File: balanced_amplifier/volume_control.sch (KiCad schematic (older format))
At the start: 49 parts, among them U5 LM4562, U6 LM4562, U7 LM4562, U8 LM4562

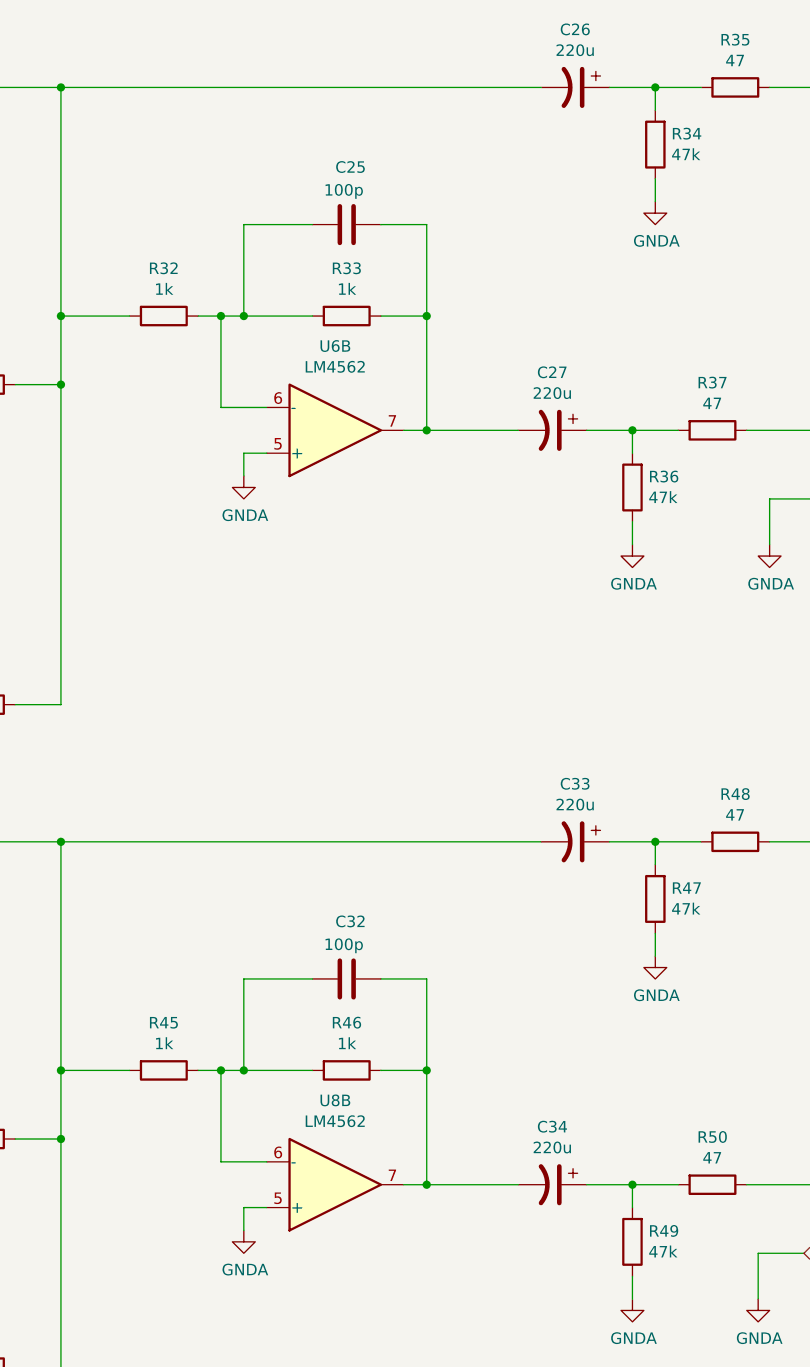
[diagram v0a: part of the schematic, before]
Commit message: Update output coupling cap to be nonpolarized and add specific part details
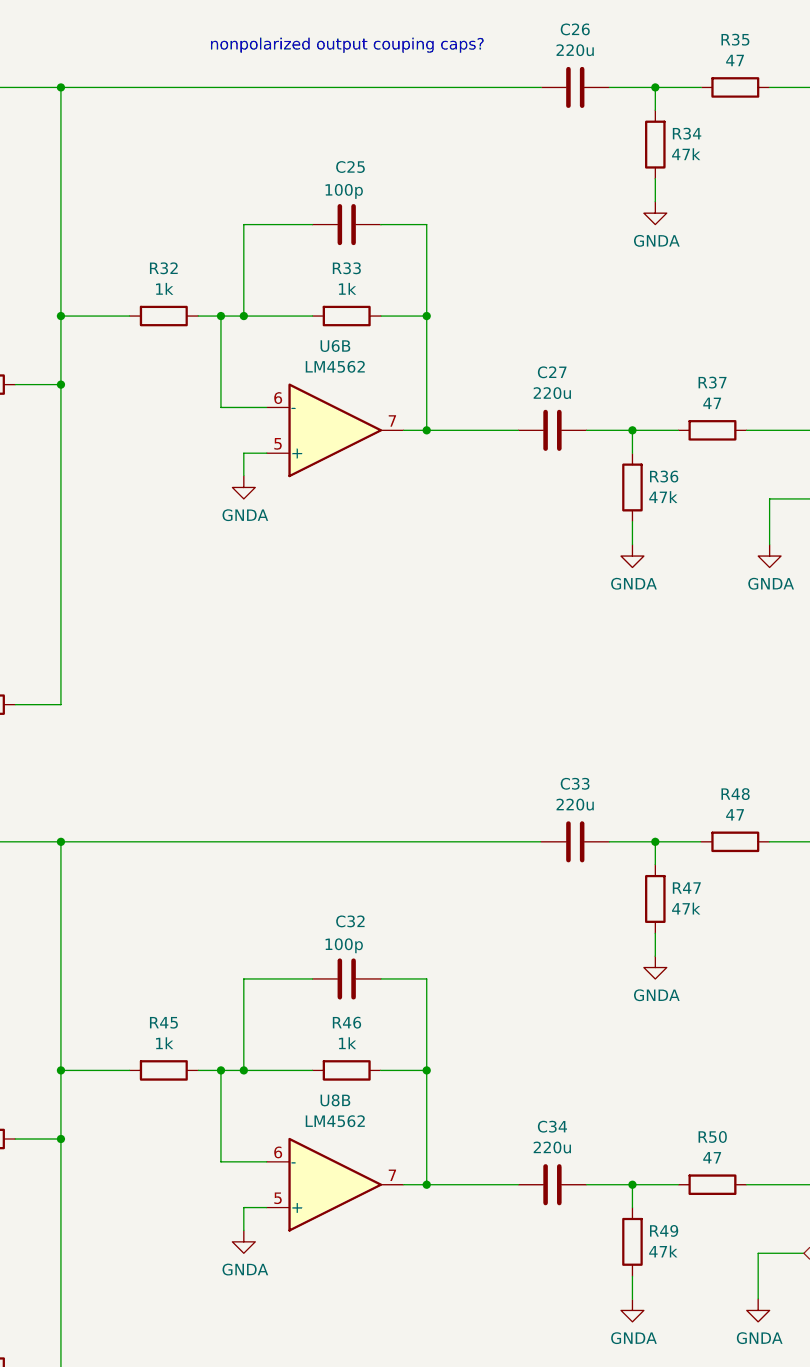
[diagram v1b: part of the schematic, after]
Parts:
- removed C26, C27, C33, C34: 220u, symbol Device:CP1
- added C26, C27, C33, C34: 220u, Capacitor_THT:C_Radial_D12.5mm_H25.0mm_P5.00mm, symbol Device:C
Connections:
- net at C25.1, R33.1, U6.7: now also C27.2
- net at R28.1, R31.1, R32.2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: now also C26.2
- net at C32.1, R46.1, U8.7: now also C34.2
- net at R41.1, R44.1, R45.2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: now also C33.2
- net at R34.2, R35.2: now also C26.1
- net at R36.2, R37.2: now also C27.1
- net at R49.2, R50.2: now also C34.1
- net at R47.2, R48.2: now also C33.1
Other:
- note added: "nonpolarized output couping caps?"
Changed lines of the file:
@@
 	8050 5200 8050 4800
-$Comp
-L Device:CP1 C34
-U 1 1 5C15C581
-P 8600 5700
-F 0 "C34" V 8348 5700 50  0000 C CNN
-F 1 "220u" V 8439 5700 50  0000 C CNN
-F 2 "" H 8600 5700 50  0001 C CNN
-F 3 "~" H 8600 5700 50  0001 C CNN
-F 4 "Electrolytic" V 8600 5700 50  0001 C CNN "Dielectric"
-F 5 "35V" V 8600 5700 50  0001 C CNN "Voltage Rating"
-	1    8600 5700
-	0    1    1    0
-$EndComp
 $Comp
 L Device:R R49
@@
 	0    -1   -1   0
 $EndComp
-$Comp
-L Device:CP1 C33
-U 1 1 5C4F3941
+Text Notes 7100 750  0    50   ~ 0
+nonpolarized output couping caps?
+$Comp
+L Device:C C?
+U 1 1 5C4F8306
+P 8700 900
+AR Path="/5C4F8306" Ref="C?"  Part="1"
+AR Path="/5BE4EEC1/5C4F8306" Ref="C?"  Part="1"
+AR Path="/5BF8808C/5C4F8306" Ref="C26"  Part="1"
+F 0 "C26" V 8448 900 50  0000 C CNN
+F 1 "220u" V 8539 900 50  0000 C CNN
+F 2 "Capacitor_THT:C_Radial_D12.5mm_H25.0mm_P5.00mm" H 8738 750 50  0001 C CNN
+F 3 "http://nichicon-us.com/english/products/pdfs/e-uvp.pdf" H 8700 900 50  0001 C CNN
+F 4 "Nichicon" H 8700 900 50  0001 C CNN "Manufacturer"
+F 5 "UVP1V221MHD" H 8700 900 50  0001 C CNN "Manufacturer PN"
+F 6 "Digikey" H 8700 900 50  0001 C CNN "Distributor"
+F 7 "493-16138-ND" H 8700 900 50  0001 C CNN "Distributor PN"
+F 8 "https://www.digikey.com/product-detail/en/nichicon/UVP1V221MHD/493-16138-ND/2539596" H 8700 900 50  0001 C CNN "URL"
+F 9 "0.87" H 8700 900 50  0001 C CNN "Unit Price"
+F 10 "Nonpolarized Electrolytic" V 8700 900 50  0001 C CNN "Dielectric"
+F 11 "35V" V 8700 900 50  0001 C CNN "Voltage Rating"
+	1    8700 900
+	0    1    1    0
+$EndComp
+$Comp
+L Device:C C?
+U 1 1 5C503D82
+P 8600 2400
+AR Path="/5C503D82" Ref="C?"  Part="1"
+AR Path="/5BE4EEC1/5C503D82" Ref="C?"  Part="1"
+AR Path="/5BF8808C/5C503D82" Ref="C27"  Part="1"
+F 0 "C27" V 8348 2400 50  0000 C CNN
+F 1 "220u" V 8439 2400 50  0000 C CNN
+F 2 "Capacitor_THT:C_Radial_D12.5mm_H25.0mm_P5.00mm" H 8638 2250 50  0001 C CNN
+F 3 "http://nichicon-us.com/english/products/pdfs/e-uvp.pdf" H 8600 2400 50  0001 C CNN
+F 4 "Nichicon" H 8600 2400 50  0001 C CNN "Manufacturer"
+F 5 "UVP1V221MHD" H 8600 2400 50  0001 C CNN "Manufacturer PN"
+F 6 "Digikey" H 8600 2400 50  0001 C CNN "Distributor"
+F 7 "493-16138-ND" H 8600 2400 50  0001 C CNN "Distributor PN"
+F 8 "https://www.digikey.com/product-detail/en/nichicon/UVP1V221MHD/493-16138-ND/2539596" H 8600 2400 50  0001 C CNN "URL"
+F 9 "0.87" H 8600 2400 50  0001 C CNN "Unit Price"
+F 10 "Nonpolarized Electrolytic" V 8600 2400 50  0001 C CNN "Dielectric"
+F 11 "35V" V 8600 2400 50  0001 C CNN "Voltage Rating"
+	1    8600 2400
+	0    1    1    0
+$EndComp
+$Comp
+L Device:C C?
+U 1 1 5C503F94
 P 8700 4200
+AR Path="/5C503F94" Ref="C?"  Part="1"
+AR Path="/5BE4EEC1/5C503F94" Ref="C?"  Part="1"
+AR Path="/5BF8808C/5C503F94" Ref="C33"  Part="1"
 F 0 "C33" V 8448 4200 50  0000 C CNN
 F 1 "220u" V 8539 4200 50  0000 C CNN
-F 2 "" H 8700 4200 50  0001 C CNN
-F 3 "~" H 8700 4200 50  0001 C CNN
-F 4 "Electrolytic" V 8700 4200 50  0001 C CNN "Dielectric"
-F 5 "35V" V 8700 4200 50  0001 C CNN "Voltage Rating"
+F 2 "Capacitor_THT:C_Radial_D12.5mm_H25.0mm_P5.00mm" H 8738 4050 50  0001 C CNN
+F 3 "http://nichicon-us.com/english/products/pdfs/e-uvp.pdf" H 8700 4200 50  0001 C CNN
+F 4 "Nichicon" H 8700 4200 50  0001 C CNN "Manufacturer"
+F 5 "UVP1V221MHD" H 8700 4200 50  0001 C CNN "Manufacturer PN"
+F 6 "Digikey" H 8700 4200 50  0001 C CNN "Distributor"
+F 7 "493-16138-ND" H 8700 4200 50  0001 C CNN "Distributor PN"
+F 8 "https://www.digikey.com/product-detail/en/nichicon/UVP1V221MHD/493-16138-ND/2539596" H 8700 4200 50  0001 C CNN "URL"
+F 9 "0.87" H 8700 4200 50  0001 C CNN "Unit Price"
+F 10 "Nonpolarized Electrolytic" V 8700 4200 50  0001 C CNN "Dielectric"
+F 11 "35V" V 8700 4200 50  0001 C CNN "Voltage Rating"
 	1    8700 4200
 	0    1    1    0
 $EndComp
 $Comp
-L Device:CP1 C27
-U 1 1 5C4F39DA
-P 8600 2400
-F 0 "C27" V 8348 2400 50  0000 C CNN
-F 1 "220u" V 8439 2400 50  0000 C CNN
-F 2 "" H 8600 2400 50  0001 C CNN
-F 3 "~" H 8600 2400 50  0001 C CNN
-F 4 "Electrolytic" V 8600 2400 50  0001 C CNN "Dielectric"
-F 5 "35V" V 8600 2400 50  0001 C CNN "Voltage Rating"
-	1    8600 2400
-	0    1    1    0
-$EndComp
-$Comp
-L Device:CP1 C26
-U 1 1 5C4F3A7A
-P 8700 900
-F 0 "C26" V 8448 900 50  0000 C CNN
-F 1 "220u" V 8539 900 50  0000 C CNN
-F 2 "" H 8700 900 50  0001 C CNN
-F 3 "~" H 8700 900 50  0001 C CNN
-F 4 "Electrolytic" V 8700 900 50  0001 C CNN "Dielectric"
-F 5 "35V" V 8700 900 50  0001 C CNN "Voltage Rating"
-	1    8700 900
-	0    1    1    0
-$EndComp
+L Device:C C?
+U 1 1 5C50403E
+P 8600 5700
+AR Path="/5C50403E" Ref="C?"  Part="1"
+AR Path="/5BE4EEC1/5C50403E" Ref="C?"  Part="1"
+AR Path="/5BF8808C/5C50403E" Ref="C34"  Part="1"
+F 0 "C34" V 8348 5700 50  0000 C CNN
+F 1 "220u" V 8439 5700 50  0000 C CNN
+F 2 "Capacitor_THT:C_Radial_D12.5mm_H25.0mm_P5.00mm" H 8638 5550 50  0001 C CNN
+F 3 "http://nichicon-us.com/english/products/pdfs/e-uvp.pdf" H 8600 5700 50  0001 C CNN
+F 4 "Nichicon" H 8600 5700 50  0001 C CNN "Manufacturer"
+F 5 "UVP1V221MHD" H 8600 5700 50  0001 C CNN "Manufacturer PN"
+F 6 "Digikey" H 8600 5700 50  0001 C CNN "Distributor"
+F 7 "493-16138-ND" H 8600 5700 50  0001 C CNN "Distributor PN"
+F 8 "https://www.digikey.com/product-detail/en/nichicon/UVP1V221MHD/493-16138-ND/2539596" H 8600 5700 50  0001 C CNN "URL"
+F 9 "0.87" H 8600 5700 50  0001 C CNN "Unit Price"
+F 10 "Nonpolarized Electrolytic" V 8600 5700 50  0001 C CNN "Dielectric"
+F 11 "35V" V 8600 5700 50  0001 C CNN "Voltage Rating"
+	1    8600 5700
+	0    1    1    0
+$EndComp

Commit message: add specific part details to capacitors
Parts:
- C22, C29: footprint (none) -> Capacitor_THT:CP_Radial_D5.0mm_P2.00mm; Distributor (none) -> Digikey; Distributor PN (none) -> 493-1077-ND; Manufacturer (none) -> Nichicon; Manufacturer PN (none) -> UVR1V100MDD; URL (none) -> https://www.digikey.com/product-detail/en/nichicon/UVR1V100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; Unit Price (none) -> 0.27
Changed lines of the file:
@@
 F 0 "C22" V 3252 1800 50  0000 C CNN
 F 1 "10u" V 3161 1800 50  0000 C CNN
-F 2 "" H 3000 1800 50  0001 C CNN
-F 3 "~" H 3000 1800 50  0001 C CNN
-F 4 "Electrolytic" V 3000 1800 50  0001 C CNN "Dielectric"
-F 5 "35V" V 3000 1800 50  0001 C CNN "Voltage Rating"
+F 2 "Capacitor_THT:CP_Radial_D5.0mm_P2.00mm" H 3000 1800 50  0001 C CNN
+F 3 "http://nichicon-us.com/english/products/pdfs/e-uvr.pdf" H 3000 1800 50  0001 C CNN
+F 4 "Nichicon" H 3000 1800 50  0001 C CNN "Manufacturer"
+F 5 "UVR1V100MDD" H 3000 1800 50  0001 C CNN "Manufacturer PN"
+F 6 "Digikey" H 3000 1800 50  0001 C CNN "Distributor"
+F 7 "493-1077-ND" H 3000 1800 50  0001 C CNN "Distributor PN"
+F 8 "https://www.digikey.com/product-detail/en/nichicon/UVR1V100MDD/493-1077-ND/588818" H 3000 1800 50  0001 C CNN "URL"
+F 9 "0.27" H 3000 1800 50  0001 C CNN "Unit Price"
+F 10 "Electrolytic" V 3000 1800 50  0001 C CNN "Dielectric"
+F 11 "35V" V 3000 1800 50  0001 C CNN "Voltage Rating"
 	1    3000 1800
 	0    -1   -1   0
@@
 F 1 "100p" V 5150 1200 50  0000 L CNN
 F 2 "Capacitor_SMD:C_0603_1608Metric_Pad1.05x0.95mm_HandSolder" H 5338 1150 50  0001 C CNN
-F 3 "~" H 5300 1300 50  0001 C CNN
+F 3 "http://www.yageo.com/documents/recent/UPY-GP_NP0_16V-to-50V_16.pdf" H 5300 1300 50  0001 C CNN
 F 4 "Yageo" H 5300 1300 50  0001 C CNN "Manufacturer"
 F 5 "CC0603JRNPO9BN101" H 5300 1300 50  0001 C CNN "Manufacturer PN"
@@
 F 1 "100p" V 5150 2600 50  0000 L CNN
 F 2 "Capacitor_SMD:C_0603_1608Metric_Pad1.05x0.95mm_HandSolder" H 5338 2550 50  0001 C CNN
-F 3 "~" H 5300 2700 50  0001 C CNN
+F 3 "http://www.yageo.com/documents/recent/UPY-GP_NP0_16V-to-50V_16.pdf" H 5300 2700 50  0001 C CNN
 F 4 "Yageo" H 5300 2700 50  0001 C CNN "Manufacturer"
 F 5 "CC0603JRNPO9BN101" H 5300 2700 50  0001 C CNN "Manufacturer PN"
@@
 F 1 "100p" V 7550 1400 50  0000 L CNN
 F 2 "Capacitor_SMD:C_0603_1608Metric_Pad1.05x0.95mm_HandSolder" H 7738 1350 50  0001 C CNN
-F 3 "~" H 7700 1500 50  0001 C CNN
+F 3 "http://www.yageo.com/documents/recent/UPY-GP_NP0_16V-to-50V_16.pdf" H 7700 1500 50  0001 C CNN
 F 4 "Yageo" H 7700 1500 50  0001 C CNN "Manufacturer"
 F 5 "CC0603JRNPO9BN101" H 7700 1500 50  0001 C CNN "Manufacturer PN"
@@
 F 1 "100p" V 5150 4500 50  0000 L CNN
 F 2 "Capacitor_SMD:C_0603_1608Metric_Pad1.05x0.95mm_HandSolder" H 5338 4450 50  0001 C CNN
-F 3 "~" H 5300 4600 50  0001 C CNN
+F 3 "http://www.yageo.com/documents/recent/UPY-GP_NP0_16V-to-50V_16.pdf" H 5300 4600 50  0001 C CNN
 F 4 "Yageo" H 5300 4600 50  0001 C CNN "Manufacturer"
 F 5 "CC0603JRNPO9BN101" H 5300 4600 50  0001 C CNN "Manufacturer PN"
@@
 F 1 "100p" V 5150 5900 50  0000 L CNN
 F 2 "Capacitor_SMD:C_0603_1608Metric_Pad1.05x0.95mm_HandSolder" H 5338 5850 50  0001 C CNN
-F 3 "~" H 5300 6000 50  0001 C CNN
+F 3 "http://www.yageo.com/documents/recent/UPY-GP_NP0_16V-to-50V_16.pdf" H 5300 6000 50  0001 C CNN
 F 4 "Yageo" H 5300 6000 50  0001 C CNN "Manufacturer"
 F 5 "CC0603JRNPO9BN101" H 5300 6000 50  0001 C CNN "Manufacturer PN"
@@
 F 1 "100p" V 7550 4700 50  0000 L CNN
 F 2 "Capacitor_SMD:C_0603_1608Metric_Pad1.05x0.95mm_HandSolder" H 7738 4650 50  0001 C CNN
-F 3 "~" H 7700 4800 50  0001 C CNN
+F 3 "http://www.yageo.com/documents/recent/UPY-GP_NP0_16V-to-50V_16.pdf" H 7700 4800 50  0001 C CNN
 F 4 "Yageo" H 7700 4800 50  0001 C CNN "Manufacturer"
 F 5 "CC0603JRNPO9BN101" H 7700 4800 50  0001 C CNN "Manufacturer PN"
@@
 Wire Wire Line
 	5750 6500 5750 6900
-$Comp
-L Device:CP1 C29
-U 1 1 5C4F35F1
-P 3000 5100
-F 0 "C29" V 3252 5100 50  0000 C CNN
-F 1 "10u" V 3161 5100 50  0000 C CNN
-F 2 "" H 3000 5100 50  0001 C CNN
-F 3 "~" H 3000 5100 50  0001 C CNN
-F 4 "Electrolytic" V 3000 5100 50  0001 C CNN "Dielectric"
-F 5 "35V" V 3000 5100 50  0001 C CNN "Voltage Rating"
-	1    3000 5100
-	0    -1   -1   0
-$EndComp
 Text Notes 7100 750  0    50   ~ 0
 nonpolarized output couping caps?
@@
 	0    1    1    0
 $EndComp
+$Comp
+L Device:CP1 C29
+U 1 1 5C505568
+P 3000 5100
+F 0 "C29" V 3252 5100 50  0000 C CNN
+F 1 "10u" V 3161 5100 50  0000 C CNN
+F 2 "Capacitor_THT:CP_Radial_D5.0mm_P2.00mm" H 3000 5100 50  0001 C CNN
+F 3 "http://nichicon-us.com/english/products/pdfs/e-uvr.pdf" H 3000 5100 50  0001 C CNN
+F 4 "Nichicon" H 3000 5100 50  0001 C CNN "Manufacturer"
+F 5 "UVR1V100MDD" H 3000 5100 50  0001 C CNN "Manufacturer PN"
+F 6 "Digikey" H 3000 5100 50  0001 C CNN "Distributor"
+F 7 "493-1077-ND" H 3000 5100 50  0001 C CNN "Distributor PN"
+F 8 "https://www.digikey.com/product-detail/en/nichicon/UVR1V100MDD/493-1077-ND/588818" H 3000 5100 50  0001 C CNN "URL"
+F 9 "0.27" H 3000 5100 50  0001 C CNN "Unit Price"
+F 10 "Electrolytic" V 3000 5100 50  0001 C CNN "Dielectric"
+F 11 "35V" V 3000 5100 50  0001 C CNN "Voltage Rating"
+	1    3000 5100
+	0    -1   -1   0
+$EndComp
 $EndSCHEMATC

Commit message: specify resistor details
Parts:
- R25, R34, R36, R38, R47, R49: Distributor (none) -> Digikey; Distributor PN (none) -> YAG3355CT-ND; Manufacturer (none) -> Yageo; Manufacturer PN (none) -> RT0603FRE0747KL; URL (none) -> https://www.digikey.com/product-detail/en/yageo/RT0603FRE07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; Unit Price (none) -> 0.10
- R26, R29, R32, R33, R39, R42, R45, R46: Distributor (none) -> Digikey; Distributor PN (none) -> YAG3366CT-ND; Manufacturer (none) -> Yageo; Manufacturer PN (none) -> RT1206FRE071KL; URL (none) -> https://www.digikey.com/product-detail/en/yageo/RT1206FRE07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; Unit Price (none) -> 0.15
- R27, R30, R40, R43: Distributor (none) -> Digikey; Distributor PN (none) -> YAG3354CT-ND; Manufacturer (none) -> Yageo; Manufacturer PN (none) -> RT0603FRE073K3L; URL (none) -> https://www.digikey.com/product-detail/en/yageo/RT0603FRE07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; Unit Price (none) -> 0.10
- R28, R31, R41, R44: Distributor (none) -> Digikey; Distributor PN (none) -> RNCP0603FTD10R0CT-ND; Manufacturer (none) -> Stackpole; Manufacturer PN (none) -> RNCP0603FTD10R0; URL (none) -> https://www.digikey.com/product-detail/en/stackpole-electro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; Unit Price (none) -> 0.10
- R35, R37, R48, R50: Distributor (none) -> Digikey; Distributor PN (none) -> 311-2593-1-ND; Manufacturer (none) -> Yageo; Manufacturer PN (none) -> RT0603DRE0747RL; URL (none) -> https://www.digikey.com/product-detail/en/yageo/RT0603DRE07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; Unit Price (none) -> 0.12

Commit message: Assign footprint to potentiometers
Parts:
- RV2: footprint (none) -> Potentiometer_THT_custom:Potentiometer_Bourns_91_Dual_Horizontal
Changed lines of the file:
@@
 F 0 "RV2" H 2630 946 50  0000 R CNN
 F 1 "5k" H 2630 855 50  0000 R CNN
-F 2 "" H 2700 900 50  0001 C CNN
+F 2 "Potentiometer_THT_custom:Potentiometer_Bourns_91_Dual_Horizontal" H 2700 900 50  0001 C CNN
 F 3 "https://www.bourns.com/docs/Product-Datasheets/91_95.pdf" H 2700 900 50  0001 C CNN
 F 4 "Bourns" H 2700 900 50  0001 C CNN "Manufacturer"
@@
 F 0 "RV2" H 2630 4246 50  0000 R CNN
 F 1 "5k" H 2630 4155 50  0000 R CNN
-F 2 "" H 2700 4200 50  0001 C CNN
+F 2 "Potentiometer_THT_custom:Potentiometer_Bourns_91_Dual_Horizontal" H 2700 4200 50  0001 C CNN
 F 3 "https://www.bourns.com/docs/Product-Datasheets/91_95.pdf" H 2700 4200 50  0001 C CNN
 F 4 "Bourns" H 2700 4200 50  0001 C CNN "Manufacturer"
